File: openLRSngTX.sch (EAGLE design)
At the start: 28 parts, among them IC1 RFM23BPSMD, J1 AVR_SPI_PRG_6PTH, Q1 MMBT2222, U1 ATMEGA328P, X1 BU-SMA-V, Y1 16MHz

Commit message: minor updates
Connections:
- net TXD: now also JP1.4; no longer JP1.5
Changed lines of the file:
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@@
 </segment>
 <segment>
-<pinref part="JP1" gate="G$1" pin="5"/>
-<wire x1="-5.08" y1="50.8" x2="-2.54" y2="50.8" width="0.1524" layer="91"/>
-<label x="-2.54" y="50.8" size="1.778" layer="95"/>
+<pinref part="JP1" gate="G$1" pin="4"/>
+<wire x1="-5.08" y1="48.26" x2="-2.54" y2="48.26" width="0.1524" layer="91"/>
+<label x="-2.54" y="48.26" size="1.778" layer="95"/>
 </segment>
 </net>

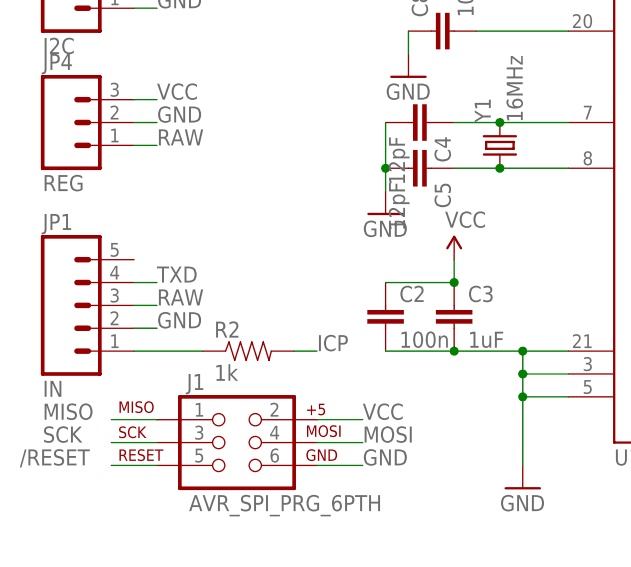
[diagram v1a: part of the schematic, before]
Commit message: Add resistor to TXD towards 'host' Add cutout over the antenna connection.
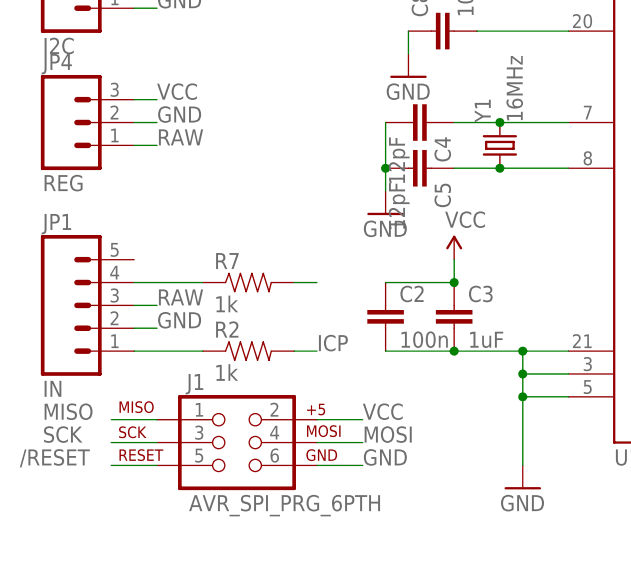
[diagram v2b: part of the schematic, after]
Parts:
- added R7: 1k, SparkFun-Resistors:RESISTOR0402-RES
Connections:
- new net N$17: JP1.4, R7.1
- net TXD: now also R7.2; no longer JP1.4
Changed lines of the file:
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@@
 <part name="GND7" library="SparkFun-Aesthetics" deviceset="GND" device=""/>
 <part name="S1" library="SparkFun-Electromechanical" deviceset="SWITCH-MOMENTARY-2" device="SMD"/>
+<part name="R7" library="SparkFun-Resistors" deviceset="RESISTOR" device="0402-RES" value="1k"/>
 </parts>
 <sheets>
@@
 <instance part="GND7" gate="1" x="25.4" y="71.12"/>
 <instance part="S1" gate="G$1" x="101.6" y="86.36"/>
+<instance part="R7" gate="G$1" x="7.62" y="48.26"/>
 </instances>
 <busses>
@@
 </segment>
 <segment>
-<pinref part="JP1" gate="G$1" pin="4"/>
-<wire x1="-5.08" y1="48.26" x2="-2.54" y2="48.26" width="0.1524" layer="91"/>
-<label x="-2.54" y="48.26" size="1.778" layer="95"/>
+<pinref part="R7" gate="G$1" pin="2"/>
+<wire x1="12.7" y1="48.26" x2="15.24" y2="48.26" width="0.1524" layer="91"/>
 </segment>
 </net>
@@
 </segment>
 </net>
+<net name="N$17" class="0">
+<segment>
+<pinref part="R7" gate="G$1" pin="1"/>
+<pinref part="JP1" gate="G$1" pin="4"/>
+<wire x1="2.54" y1="48.26" x2="-5.08" y2="48.26" width="0.1524" layer="91"/>
+</segment>
+</net>

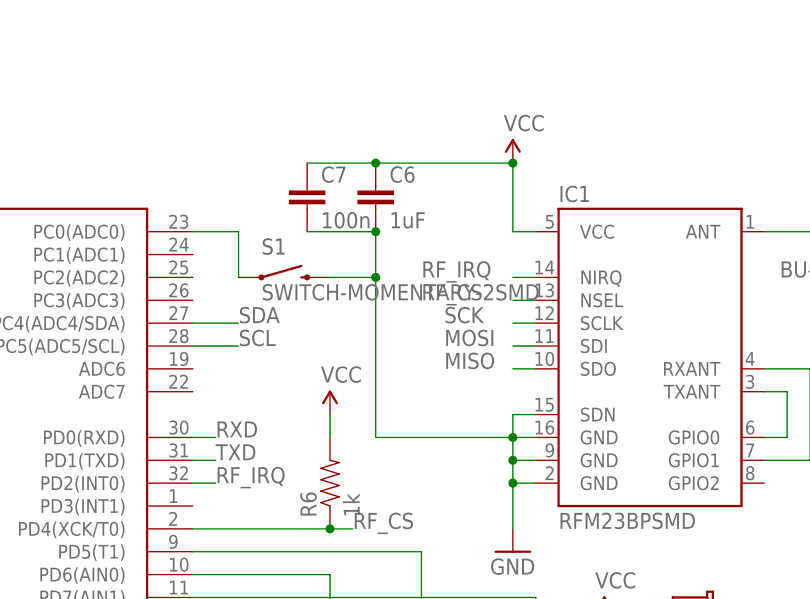
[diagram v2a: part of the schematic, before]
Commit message: Add mode switch header and room for the actual switch.
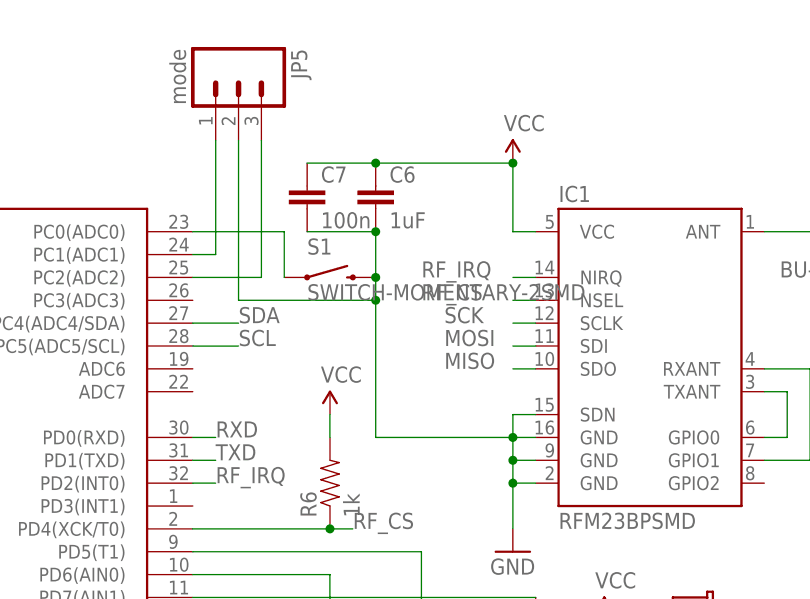
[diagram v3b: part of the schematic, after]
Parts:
- added JP5: mode, SparkFun-Connectors:M03PTH
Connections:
- new net N$18: JP5.1, U1.PC1(ADC1)
- new net N$19: JP5.3, U1.PC2(ADC2)
- net GND: now also JP5.2
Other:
- moved on the sheet: S1
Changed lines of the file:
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@@
 <part name="S1" library="SparkFun-Electromechanical" deviceset="SWITCH-MOMENTARY-2" device="SMD"/>
 <part name="R7" library="SparkFun-Resistors" deviceset="RESISTOR" device="0402-RES" value="1k"/>
+<part name="JP5" library="SparkFun-Connectors" deviceset="M03" device="PTH" value="mode"/>
 </parts>
 <sheets>
@@
 <instance part="C8" gate="G$1" x="30.48" y="76.2" rot="R90"/>
 <instance part="GND7" gate="1" x="25.4" y="71.12"/>
-<instance part="S1" gate="G$1" x="101.6" y="86.36"/>
+<instance part="S1" gate="G$1" x="106.68" y="86.36"/>
 <instance part="R7" gate="G$1" x="7.62" y="48.26"/>
+<instance part="JP5" gate="G$1" x="96.52" y="109.22" rot="R270"/>
 </instances>
 <busses>
@@
 <wire x1="127" y1="68.58" x2="111.76" y2="68.58" width="0.1524" layer="91"/>
 <pinref part="C6" gate="G$1" pin="2"/>
-<wire x1="111.76" y1="68.58" x2="111.76" y2="86.36" width="0.1524" layer="91"/>
+<wire x1="111.76" y1="68.58" x2="111.76" y2="83.82" width="0.1524" layer="91"/>
 <pinref part="C7" gate="G$1" pin="2"/>
+<wire x1="111.76" y1="83.82" x2="111.76" y2="86.36" width="0.1524" layer="91"/>
 <wire x1="111.76" y1="86.36" x2="111.76" y2="91.44" width="0.1524" layer="91"/>
 <wire x1="111.76" y1="91.44" x2="104.14" y2="91.44" width="0.1524" layer="91"/>
 <junction x="111.76" y="91.44"/>
 <pinref part="S1" gate="G$1" pin="2"/>
-<wire x1="106.68" y1="86.36" x2="111.76" y2="86.36" width="0.1524" layer="91"/>
 <junction x="111.76" y="86.36"/>
+<pinref part="JP5" gate="G$1" pin="2"/>
+<wire x1="96.52" y1="101.6" x2="96.52" y2="83.82" width="0.1524" layer="91"/>
+<wire x1="96.52" y1="83.82" x2="111.76" y2="83.82" width="0.1524" layer="91"/>
+<junction x="111.76" y="83.82"/>
 </segment>
 <segment>
@@
 <segment>
 <pinref part="S1" gate="G$1" pin="1"/>
-<wire x1="96.52" y1="86.36" x2="96.52" y2="91.44" width="0.1524" layer="91"/>
+<wire x1="101.6" y1="86.36" x2="101.6" y2="91.44" width="0.1524" layer="91"/>
 <pinref part="U1" gate="G$1" pin="PC0(ADC0)"/>
-<wire x1="96.52" y1="91.44" x2="91.44" y2="91.44" width="0.1524" layer="91"/>
+<wire x1="101.6" y1="91.44" x2="91.44" y2="91.44" width="0.1524" layer="91"/>
 </segment>
 </net>
@@
 </segment>
 </net>
+<net name="N$18" class="0">
+<segment>
+<pinref part="U1" gate="G$1" pin="PC1(ADC1)"/>
+<wire x1="91.44" y1="88.9" x2="93.98" y2="88.9" width="0.1524" layer="91"/>
+<wire x1="93.98" y1="88.9" x2="93.98" y2="101.6" width="0.1524" layer="91"/>
+<pinref part="JP5" gate="G$1" pin="1"/>
+</segment>
+</net>
+<net name="N$19" class="0">
+<segment>
+<pinref part="U1" gate="G$1" pin="PC2(ADC2)"/>
+<pinref part="JP5" gate="G$1" pin="3"/>
+<wire x1="91.44" y1="86.36" x2="99.06" y2="86.36" width="0.1524" layer="91"/>
+<wire x1="99.06" y1="86.36" x2="99.06" y2="101.6" width="0.1524" layer="91"/>
+</segment>
+</net>

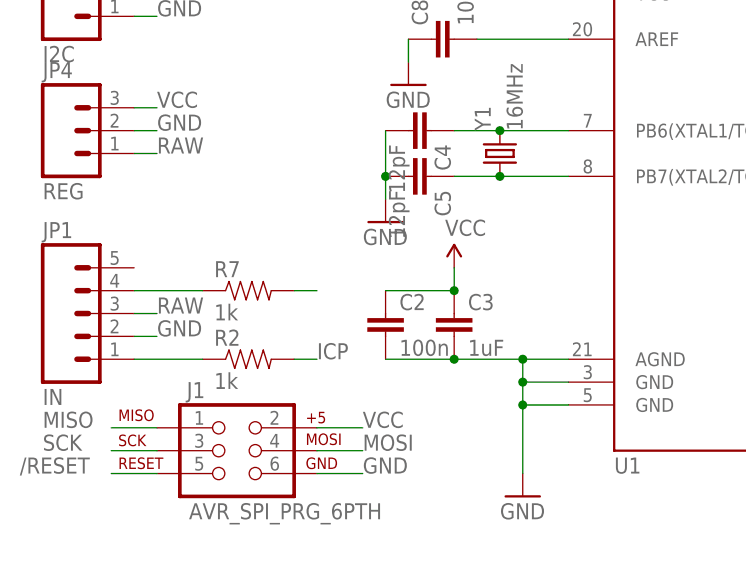
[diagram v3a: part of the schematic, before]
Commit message: Add logo on other side too.
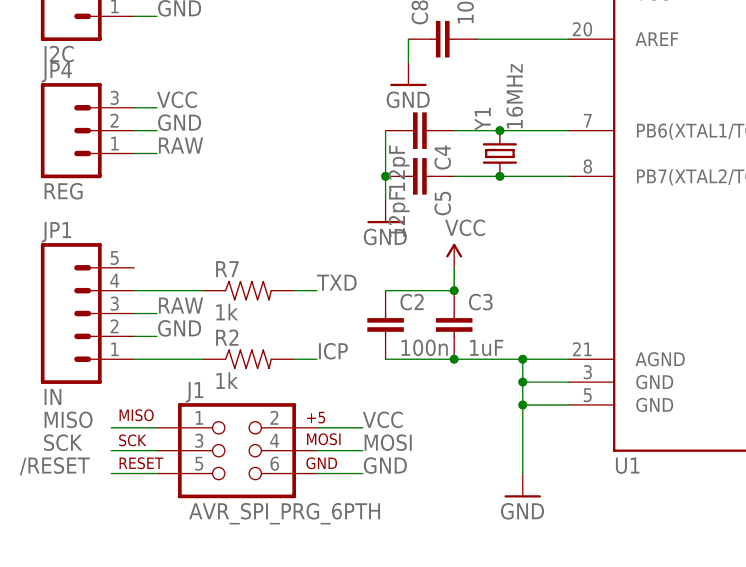
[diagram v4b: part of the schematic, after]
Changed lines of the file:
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@@
 <pinref part="R7" gate="G$1" pin="2"/>
 <wire x1="12.7" y1="48.26" x2="15.24" y2="48.26" width="0.1524" layer="91"/>
+<label x="15.24" y="48.26" size="1.778" layer="95"/>
 </segment>
 </net>

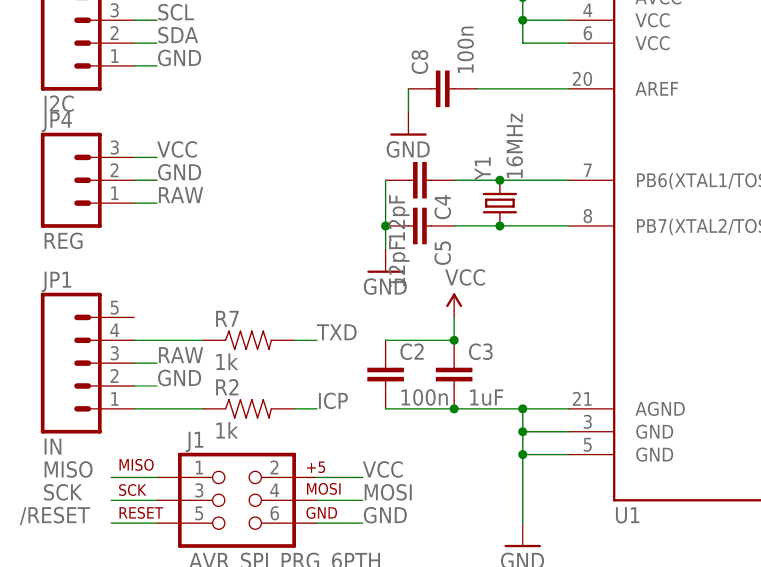
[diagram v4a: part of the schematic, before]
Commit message: Added connection for RXD towards the radio. Connected xtal case to GND. Performed some routing cleanup.
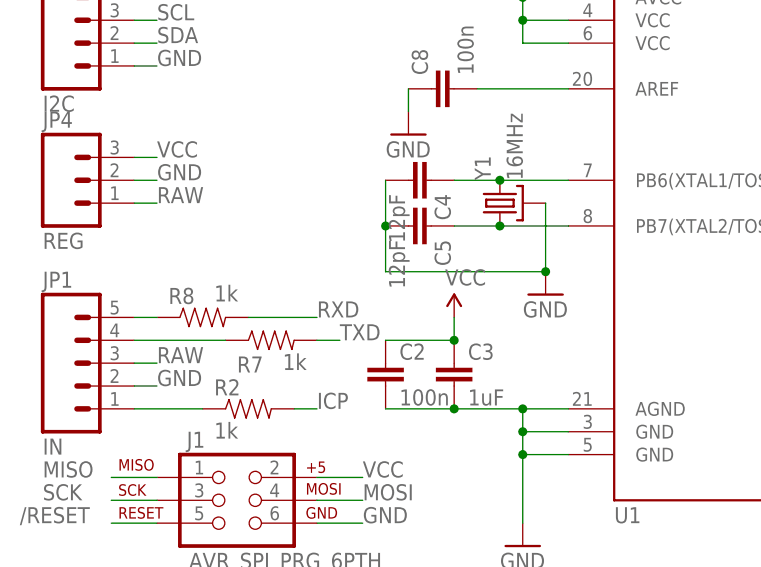
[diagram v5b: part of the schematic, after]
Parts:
- added R8: 1k, SparkFun-Resistors:RESISTOR0402-RES
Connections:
- new net N$20: JP1.5, R8.1
- net GND: now also Y1.GND
- net RXD: now also R8.2
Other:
- moved on the sheet: R7
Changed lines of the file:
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@@
 <part name="R7" library="SparkFun-Resistors" deviceset="RESISTOR" device="0402-RES" value="1k"/>
 <part name="JP5" library="SparkFun-Connectors" deviceset="M03" device="PTH" value="mode"/>
+<part name="R8" library="SparkFun-Resistors" deviceset="RESISTOR" device="0402-RES" value="1k"/>
 </parts>
 <sheets>
@@
 <instance part="C4" gate="G$1" x="25.4" y="66.04" rot="R270"/>
 <instance part="C5" gate="G$1" x="25.4" y="60.96" rot="R270"/>
-<instance part="GND5" gate="1" x="22.86" y="55.88"/>
+<instance part="GND5" gate="1" x="40.64" y="53.34"/>
 <instance part="X1" gate="G$1" x="165.1" y="91.44" rot="MR0"/>
 <instance part="GND6" gate="1" x="162.56" y="81.28"/>
@@
 <instance part="GND7" gate="1" x="25.4" y="71.12"/>
 <instance part="S1" gate="G$1" x="106.68" y="86.36"/>
-<instance part="R7" gate="G$1" x="7.62" y="48.26"/>
+<instance part="R7" gate="G$1" x="10.16" y="48.26" smashed="yes">
+<attribute name="NAME" x="6.35" y="44.6786" size="1.778" layer="95"/>
+<attribute name="VALUE" x="11.43" y="44.958" size="1.778" layer="96"/>
+</instance>
 <instance part="JP5" gate="G$1" x="96.52" y="109.22" rot="R270"/>
+<instance part="R8" gate="G$1" x="2.54" y="50.8" smashed="yes">
+<attribute name="NAME" x="-1.27" y="52.2986" size="1.778" layer="95"/>
+<attribute name="VALUE" x="3.81" y="52.578" size="1.778" layer="96"/>
+</instance>
 </instances>
 <busses>
@@
 <pinref part="GND5" gate="1" pin="GND"/>
 <pinref part="C5" gate="G$1" pin="2"/>
-<wire x1="22.86" y1="58.42" x2="22.86" y2="60.96" width="0.1524" layer="91"/>
+<wire x1="40.64" y1="55.88" x2="22.86" y2="55.88" width="0.1524" layer="91"/>
+<wire x1="22.86" y1="55.88" x2="22.86" y2="60.96" width="0.1524" layer="91"/>
 <pinref part="C4" gate="G$1" pin="2"/>
 <wire x1="22.86" y1="66.04" x2="22.86" y2="60.96" width="0.1524" layer="91"/>
 <junction x="22.86" y="60.96"/>
+<pinref part="Y1" gate="G$1" pin="GND"/>
+<wire x1="40.64" y1="55.88" x2="40.64" y2="63.5" width="0.1524" layer="91"/>
+<junction x="40.64" y="55.88"/>
 </segment>
 <segment>
@@
 <label x="93.98" y="68.58" size="1.778" layer="95"/>
 </segment>
+<segment>
+<pinref part="R8" gate="G$1" pin="2"/>
+<wire x1="7.62" y1="50.8" x2="15.24" y2="50.8" width="0.1524" layer="91"/>
+<label x="15.24" y="50.8" size="1.778" layer="95"/>
+</segment>
 </net>
 <net name="TXD" class="0">
@@
 <segment>
 <pinref part="R7" gate="G$1" pin="2"/>
-<wire x1="12.7" y1="48.26" x2="15.24" y2="48.26" width="0.1524" layer="91"/>
-<label x="15.24" y="48.26" size="1.778" layer="95"/>
+<wire x1="15.24" y1="48.26" x2="17.78" y2="48.26" width="0.1524" layer="91"/>
+<label x="17.78" y="48.26" size="1.778" layer="95"/>
 </segment>
 </net>
@@
 <pinref part="R7" gate="G$1" pin="1"/>
 <pinref part="JP1" gate="G$1" pin="4"/>
-<wire x1="2.54" y1="48.26" x2="-5.08" y2="48.26" width="0.1524" layer="91"/>
+<wire x1="5.08" y1="48.26" x2="-5.08" y2="48.26" width="0.1524" layer="91"/>
 </segment>
 </net>
@@
 </segment>
 </net>
+<net name="N$20" class="0">
+<segment>
+<pinref part="R8" gate="G$1" pin="1"/>
+<pinref part="JP1" gate="G$1" pin="5"/>
+<wire x1="-2.54" y1="50.8" x2="-5.08" y2="50.8" width="0.1524" layer="91"/>
+</segment>
+</net>

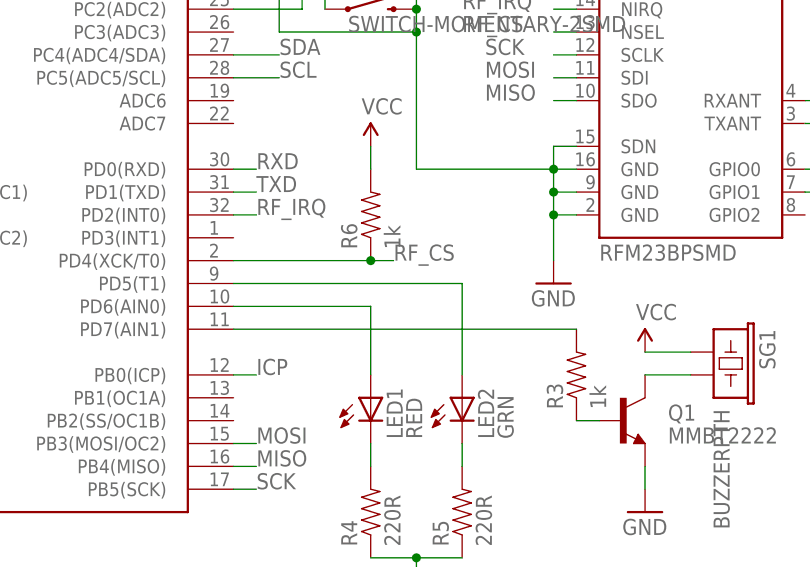
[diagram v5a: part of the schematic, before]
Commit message: Fix buzzer to correct pin.
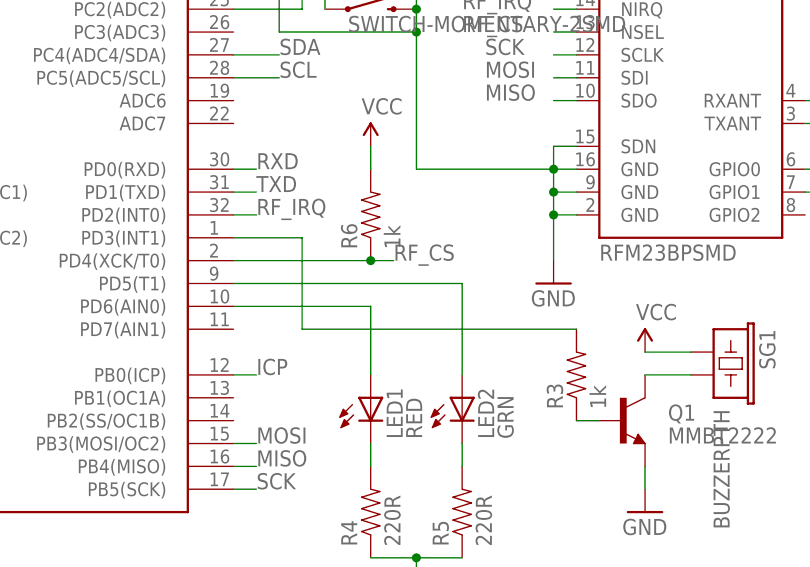
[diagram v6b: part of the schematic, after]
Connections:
- net N$4: now also U1.PD3(INT1); no longer U1.PD7(AIN1)
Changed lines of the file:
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@@
-</segment>
-</net>
-<net name="N$4" class="0">
-<segment>
-<pinref part="R3" gate="G$1" pin="2"/>
-<pinref part="U1" gate="G$1" pin="PD7(AIN1)"/>
-<wire x1="129.54" y1="50.8" x2="91.44" y2="50.8" width="0.1524" layer="91"/>
 </segment>
 </net>
@@
 </segment>
 </net>
+<net name="N$4" class="0">
+<segment>
+<pinref part="R3" gate="G$1" pin="2"/>
+<wire x1="129.54" y1="50.8" x2="99.06" y2="50.8" width="0.1524" layer="91"/>
+<wire x1="99.06" y1="50.8" x2="99.06" y2="60.96" width="0.1524" layer="91"/>
+<pinref part="U1" gate="G$1" pin="PD3(INT1)"/>
+<wire x1="99.06" y1="60.96" x2="91.44" y2="60.96" width="0.1524" layer="91"/>
+</segment>
+</net>
